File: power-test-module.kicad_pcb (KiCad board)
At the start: 2 copper layers, 38.4 x 23.9 mm, 42 parts, among them J1001 Conn_02x06_Odd_Even, J1002 USB_miniB, J1003 USB_C_Receptacle_USB2.0, U1001 USB3740B-AI9, U1002 UTC2000, U1003 FT232RL, U1004 74LVC1G00, U1005 SC185

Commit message: added part numbers for EMI filter + LEDs;
Also changed reset pullup from 4k7 to 5k1 (for sake of fewer different values)
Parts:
- R1010: value R4k7 -> 5k1

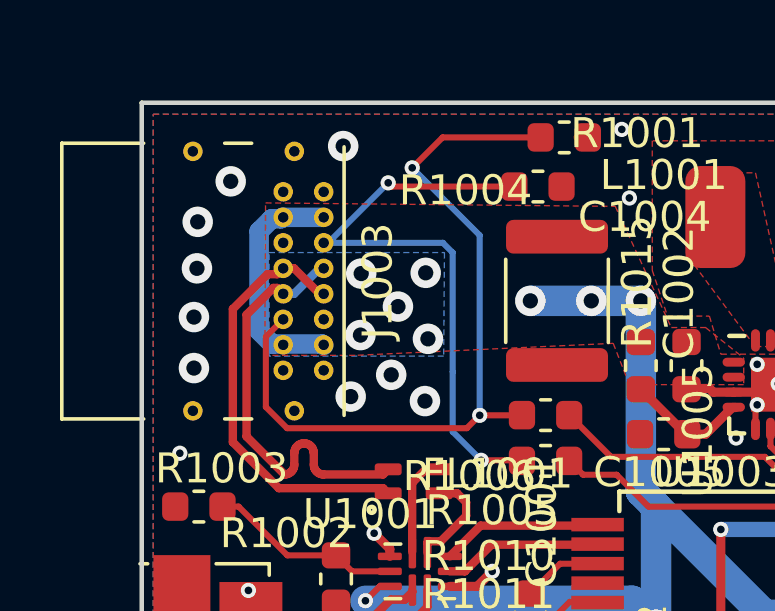
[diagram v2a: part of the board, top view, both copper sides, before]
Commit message: PCB: fixed USB4085 footprint; has wrong slits
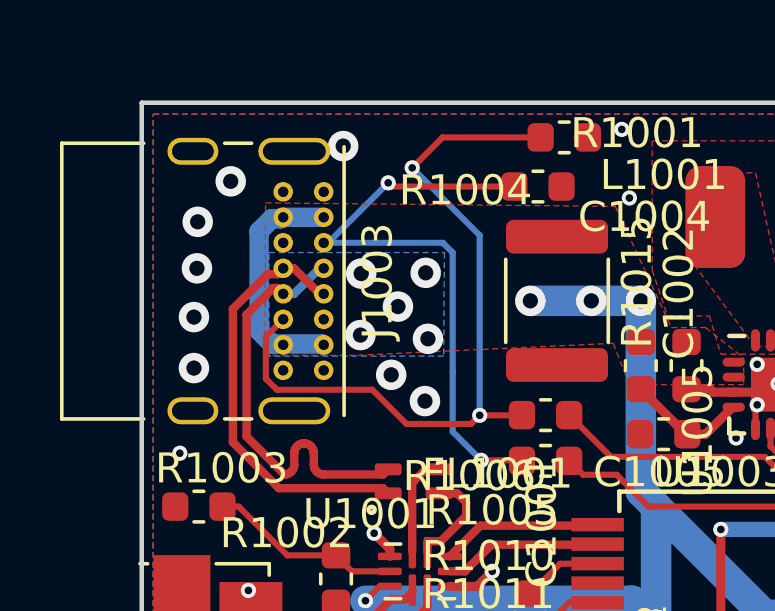
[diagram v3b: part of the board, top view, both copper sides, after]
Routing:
- net Net-(J1003-PadB5): track 26.0 -> 25.4 mm
- net GND: vias 47 -> 46
